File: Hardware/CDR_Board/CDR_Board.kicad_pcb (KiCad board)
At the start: 2 copper layers, 61 x 40.6 mm, 55 parts, among them J1 BLE Friend, J2 nRF24L01, J3 Battery, J5 USB_C_Receptacle_USB2.0, Q1 DMP2045U, SW1 BOOTSEL, SW2 RESET, U1 W25Q32JVSS, U2 SOT23-5 200mA 3.3V, U3 RP2040, U4 BQ25172, U6 ADXL343, Y1 Crystal

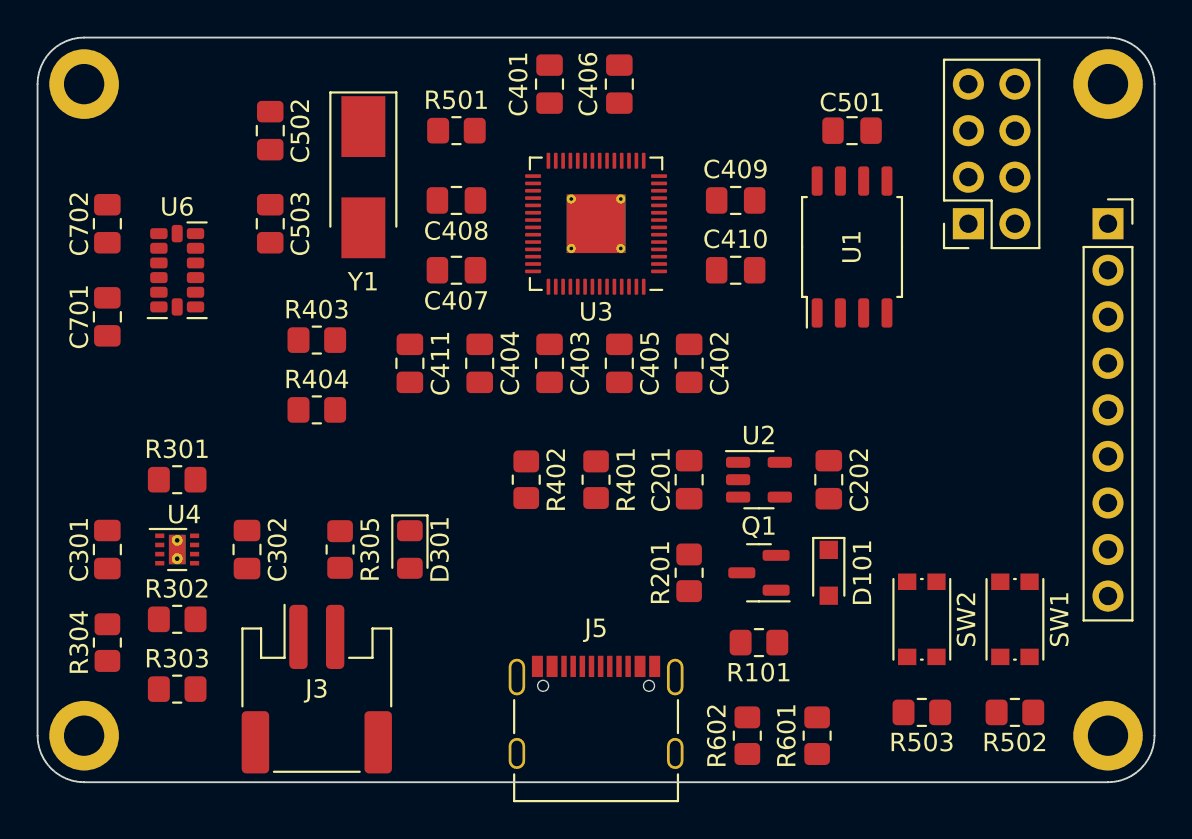
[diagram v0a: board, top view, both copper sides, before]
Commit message: CDR Board Placement Revision
Some things on 25 mil grid, 0603 capacitors for RP2040 decoupling.
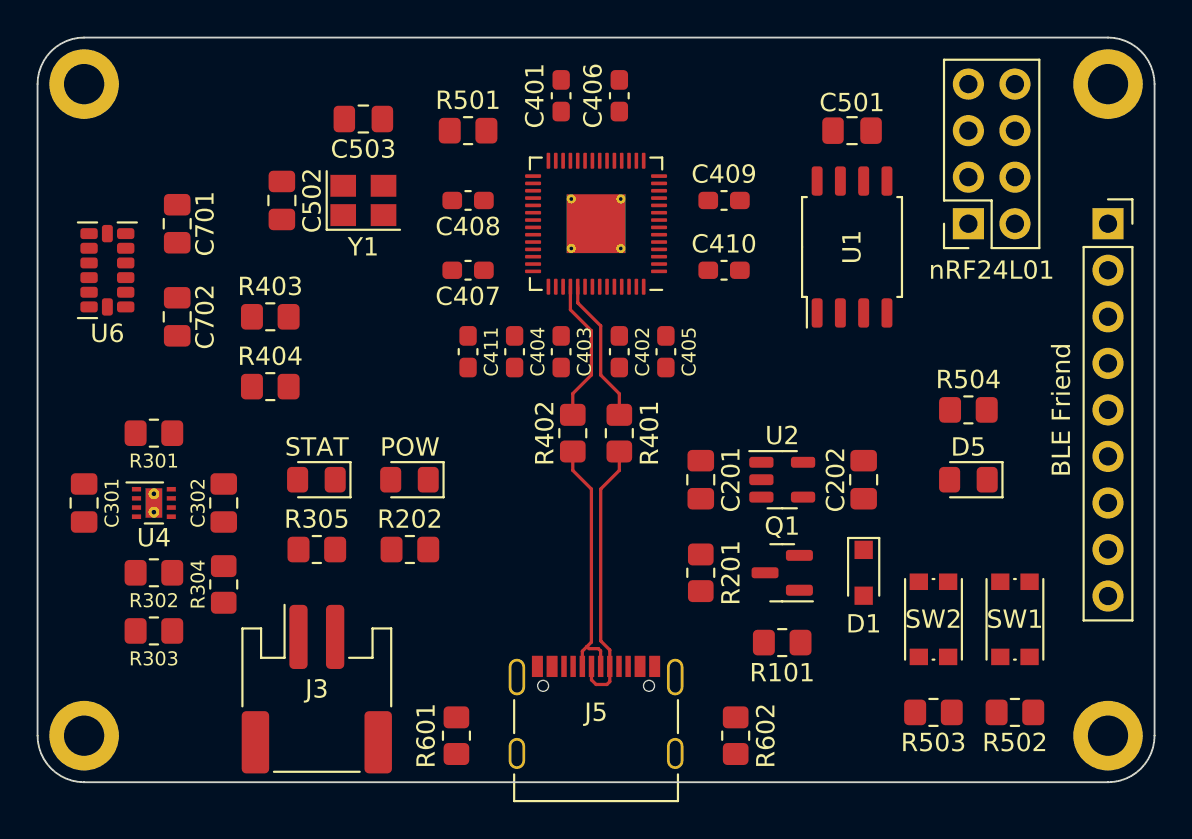
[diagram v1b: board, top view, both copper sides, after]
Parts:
- removed D101: SMB ≥20V ≥1A, Diode_SMD:D_SOD-323_HandSoldering
- removed D301: LED, LED_SMD:LED_0805_2012Metric_Pad1.15x1.40mm_HandSolder
- added D1: SMB ≥20V ≥1A, Diode_SMD:D_SOD-323_HandSoldering, F.Cu at (167.0, 105.4)
- added D2: LED, LED_SMD:LED_0805_2012Metric_Pad1.15x1.40mm_HandSolder, F.Cu at (137.1, 100.3)
- added D3: GPIO, LED_SMD:LED_0805_2012Metric_Pad1.15x1.40mm_HandSolder, F.Cu at (172.7, 100.3)
- added D4: POW, LED_SMD:LED_0805_2012Metric_Pad1.15x1.40mm_HandSolder, F.Cu at (142.2, 100.3)
- added R202: 330, Resistor_SMD:R_0805_2012Metric_Pad1.20x1.40mm_HandSolder, F.Cu at (142.2, 104.1)
- added R504: 330, Resistor_SMD:R_0805_2012Metric_Pad1.20x1.40mm_HandSolder, F.Cu at (172.7, 96.5)
- C401, C402, C403, C404, C405, C406, C407, C408, C409, C410, C411: footprint Capacitor_SMD:C_0805_2012Metric_Pad1.18x1.45mm_HandSolder -> Capacitor_SMD:C_0603_1608Metric_Pad1.08x0.95mm_HandSolder
- Y1: footprint Crystal:Crystal_SMD_Abracon_ABM3-2Pin_5.0x3.2mm_HandSoldering -> Crystal:Crystal_SMD_SeikoEpson_FA238-4Pin_3.2x2.5mm
- moved R601 19.7 mm to (144.8, 114.3)
- moved C503 7.65 mm to (139.7, 80.6), turned to 0 degrees
- moved R304 7.10 mm to (132.1, 106.0), turned to -90 degrees
- moved C701 6.35 mm to (129.5, 86.4), turned to -90 degrees
- moved C702 6.35 mm to (129.5, 91.4), turned to 90 degrees
- moved C402 3.86 mm to (153.7, 93.3)
- moved C502 3.86 mm to (135.3, 85.1)
- moved U6 3.81 mm to (125.7, 88.9), turned to 180 degrees
- moved R402 3.59 mm to (151.1, 97.8)
- moved R303 3.42 mm to (128.3, 108.6)
- moved C411 3.24 mm to (145.4, 93.3)
- moved C301 2.84 mm to (124.5, 101.6)
- moved C302 2.84 mm to (132.1, 101.6)
- moved R302 2.84 mm to (128.3, 105.4)
- moved U4 2.84 mm to (128.3, 101.6)
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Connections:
- Y1 pad 2: Net-(C503-Pad2) -> GND
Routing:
- net /D+: track 0.00 -> 15.1 mm
- net /D-: track 0.00 -> 14.0 mm
- net Net-(R401-Pad1): track 0.00 -> 7.93 mm
- net Net-(R402-Pad1): track 0.00 -> 7.89 mm
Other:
- board text added: "BLE Friend"
- board text added: "D5"
- board text added: "POW"
- board text added: "STAT"
- board text added: "nRF24L01"

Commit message: Added critical traces
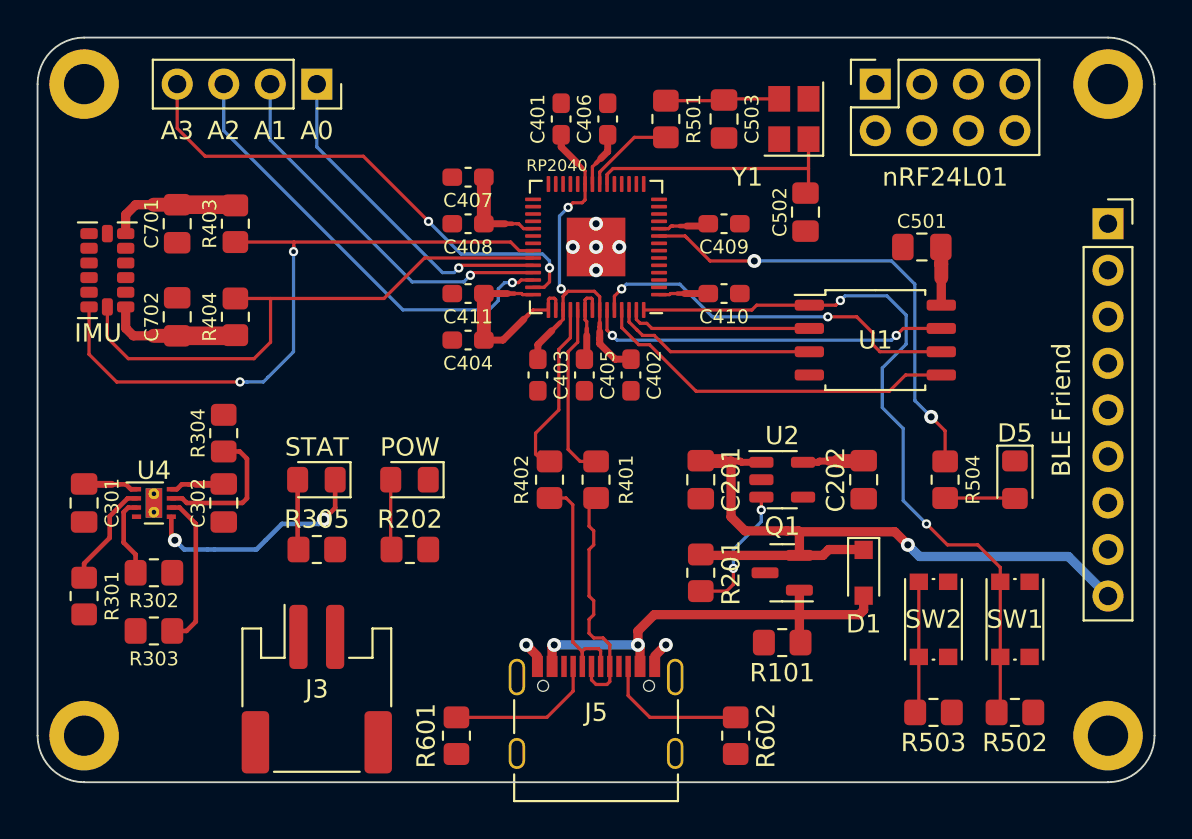
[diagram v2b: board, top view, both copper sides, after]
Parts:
- added J4: ADC, Connector_PinSocket_2.54mm:PinSocket_1x04_P2.54mm_Vertical, F.Cu at (137.2, 78.7)
- U3: footprint Package_DFN_QFN:QFN-56-1EP_7x7mm_P0.4mm_EP3.2x3.2mm_ThermalVias -> Package_DFN_QFN:QFN-56-1EP_7x7mm_P0.4mm_EP3.2x3.2mm
- moved C502 28.6 mm to (163.8, 85.7), turned to 90 degrees
- moved Y1 23.9 mm to (163.2, 80.6), turned to 90 degrees
- moved C503 19.7 mm to (159.4, 80.6), turned to 90 degrees
- moved R501 10.8 mm to (156.2, 80.6), turned to -90 degrees
- moved R301 9.67 mm to (124.5, 106.7), turned to -90 degrees
- moved J2 9.16 mm to (167.6, 78.7), turned to 90 degrees
- moved R304 8.25 mm to (132.1, 97.8)
- moved C501 7.41 mm to (170.2, 87.6), turned to 0 degrees
- moved R403 5.43 mm to (132.7, 86.4), turned to -90 degrees
- moved U1 5.24 mm to (167.6, 92.7), turned to 0 degrees
- moved C407 5.08 mm to (145.4, 83.8)
- moved C405 4.62 mm to (151.8, 94.6)
- moved R404 4.26 mm to (132.7, 91.4), turned to 90 degrees
- moved R504 4.02 mm to (171.4, 100.3), turned to 90 degrees
- moved C411 3.17 mm to (145.4, 90.2), turned to 180 degrees
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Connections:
- J1 pad 1: unconnected-(J1-Pad1) -> /SCK
- J1 pad 2: unconnected-(J1-Pad2) -> /MISO
- J1 pad 3: unconnected-(J1-Pad3) -> /MOSI
- J1 pad 4: unconnected-(J1-Pad4) -> /BLE_CS
- J1 pad 5: unconnected-(J1-Pad5) -> /BLE_IRQ
- J1 pad 8: unconnected-(J1-Pad8) -> GND
- J1 pad 9: unconnected-(J1-Pad9) -> /VSRC
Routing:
- net +3V3: track 0.00 -> 50.6 mm
- net /BOOT/FLASH_CS: track 0.00 -> 41.0 mm, vias 0 -> 2
- net /VSRC: track 0.00 -> 39.1 mm, vias 0 -> 1
- net /SDA: track 0.00 -> 37.5 mm, vias 0 -> 2
- net /SCL: track 0.00 -> 31.0 mm
- net /A3: track 0.00 -> 27.9 mm, vias 0 -> 2
- net VBUS: track 0.00 -> 27.3 mm, vias 0 -> 2
- net /D5: track 0.00 -> 25.4 mm, vias 0 -> 2
- net /A2: track 0.00 -> 24.5 mm, vias 0 -> 1
- net +1V1: track 0.00 -> 21.1 mm, vias 0 -> 2
- net /A1: track 0.00 -> 20.8 mm, vias 0 -> 1
- net /FLASH_CLK: track 0.00 -> 20.8 mm, vias 0 -> 2
- net Net-(U1-Pad5): track 0.00 -> 20.2 mm
- net Net-(U1-Pad7): track 0.00 -> 19.8 mm, vias 0 -> 2
- net /A0: track 0.00 -> 18.2 mm, vias 0 -> 1
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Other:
- board text added: "A0"
- board text added: "A1"
- board text added: "A2"
- board text added: "A3"
- board text added: "IMU"
- board text added: "RP2040"

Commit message: Finished all routing
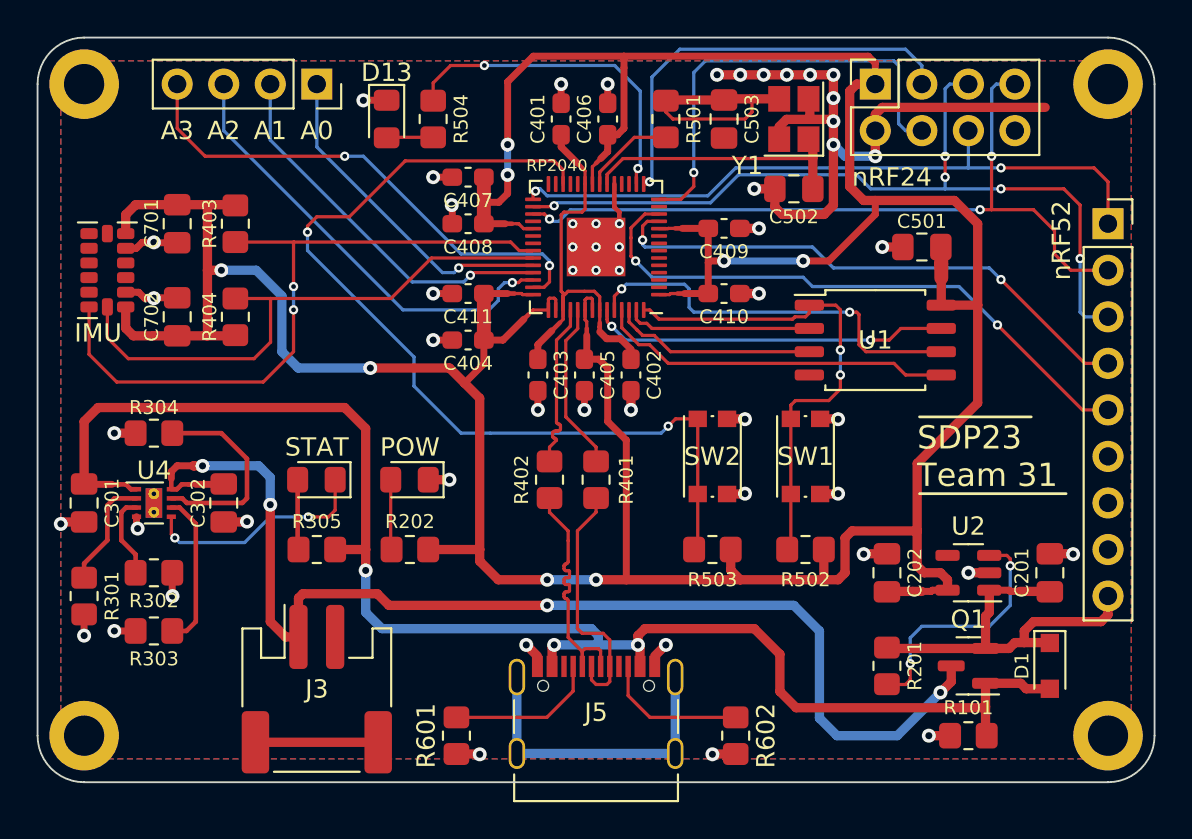
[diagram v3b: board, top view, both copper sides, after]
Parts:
- D2: value LED -> STAT
- moved D3 39.5 mm to (141.0, 80.6)
- moved R504 34.2 mm to (143.5, 80.6)
- moved C201 19.7 mm to (177.2, 105.4), turned to 90 degrees
- moved R503 15.0 mm to (158.8, 104.1)
- moved SW2 15.0 mm to (158.8, 99.1)
- moved R502 14.5 mm to (163.8, 104.1)
- moved SW1 14.5 mm to (163.8, 99.1)
- moved D1 11.4 mm to (177.2, 110.5)
- moved Q1 11.4 mm to (172.7, 110.5)
- moved R101 11.4 mm to (172.7, 114.3)
- moved R201 11.4 mm to (168.3, 110.5)
- moved U2 11.4 mm to (172.7, 105.4), turned to 180 degrees
- moved C202 5.24 mm to (168.3, 105.4), turned to 90 degrees
- moved R304 3.81 mm to (128.3, 97.8), turned to 0 degrees
- moved C502 1.42 mm to (163.2, 84.5), turned to 0 degrees
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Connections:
- J2 pad 1: unconnected-(J2-Pad1) -> +3V3
- J2 pad 2: unconnected-(J2-Pad2) -> GND
- J2 pad 3: unconnected-(J2-Pad3) -> /RF_CNS
- J2 pad 4: unconnected-(J2-Pad4) -> /RF_CE
- J2 pad 5: unconnected-(J2-Pad5) -> /MOSI
- J2 pad 6: unconnected-(J2-Pad6) -> /SCK
- J2 pad 7: unconnected-(J2-Pad7) -> /MISO
- R504 pad 2: /D5 -> /D13
- U3 pad 11: /D6 -> /BLE_CS
- U3 pad 12: /D9 -> /BLE_IRQ
- U3 pad 14: /D11 -> /RF_CE
- U3 pad 15: /D12 -> /RF_CNS
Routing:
- net +3V3: track 50.6 -> 223.3 mm, vias 0 -> 8
- net GND: track 2.85 -> 83.8 mm, vias 7 -> 55
- net +BATT: track 2.98 -> 65.4 mm, vias 0 -> 4
- net VBUS: track 27.3 -> 84.1 mm, vias 2 -> 3
- net /MOSI: track 0.00 -> 45.6 mm, vias 0 -> 5
- net /RUN: track 7.21 -> 51.6 mm, vias 0 -> 2
- net /MISO: track 0.00 -> 41.9 mm, vias 0 -> 3
- net /SCK: track 0.00 -> 37.2 mm, vias 0 -> 2
- net /BLE_IRQ: track 0.00 -> 32.9 mm, vias 0 -> 2
- net /BLE_CS: track 0.00 -> 30.1 mm, vias 0 -> 2
- net /D5: track 25.4 -> 0.00 mm, vias 2 -> 0
- net /RF_CE: track 0.00 -> 24.6 mm, vias 0 -> 1
- net /RF_CNS: track 0.00 -> 22.9 mm, vias 0 -> 1
- net /D13: track 0.00 -> 18.4 mm, vias 0 -> 2
- net unconnected-(J5-PadS1): track 0.00 -> 17.0 mm
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- added copper zone on B.Cu, net GND
- added copper zone on F.Cu, net GND
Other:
- board text added: "D13"
- board text added: "SDP23 Team 31"
- board text added: "nRF24"
- board text added: "nRF52"
- board text removed: "BLE Friend"
- board text removed: "D5"
- board text removed: "nRF24L01"

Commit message: Added stitching vias
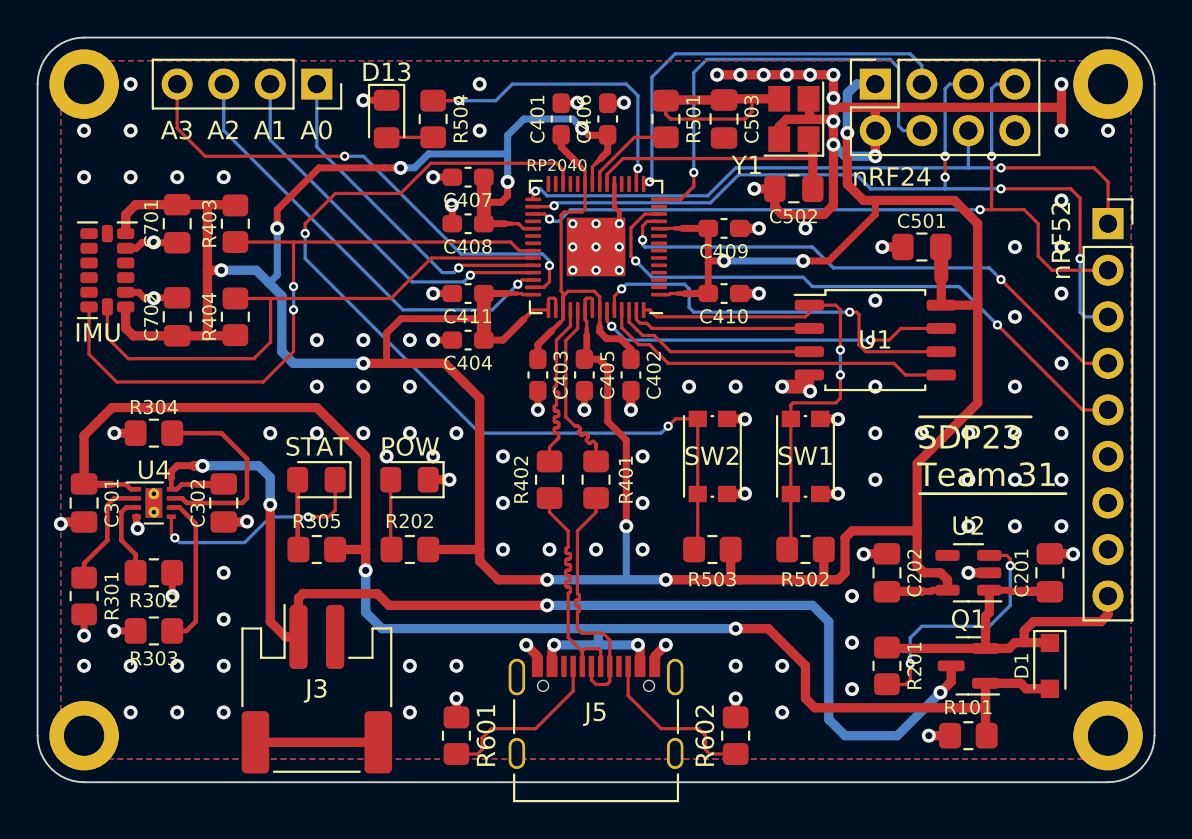
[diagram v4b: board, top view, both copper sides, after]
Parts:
- turned R601 to -90 degrees
- turned R602 to -90 degrees
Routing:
- net unconnected-(J5-PadS1): track 17.0 -> 0.00 mm
- net GND: track 83.8 -> 91.4 mm, vias 55 -> 132
- net /D13: track 18.4 -> 16.7 mm
- net Net-(J5-PadB5): track 7.95 -> 9.23 mm
- net +3V3: track 223.3 -> 222.1 mm, vias 8 -> 12
- net Net-(J5-PadA5): track 8.31 -> 9.51 mm
- net Net-(R401-Pad1): track 9.22 -> 10.1 mm
- net Net-(R402-Pad1): track 9.29 -> 10.1 mm
- net VBUS: track 84.1 -> 84.4 mm, vias 3 -> 4

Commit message: Added more stitching vias
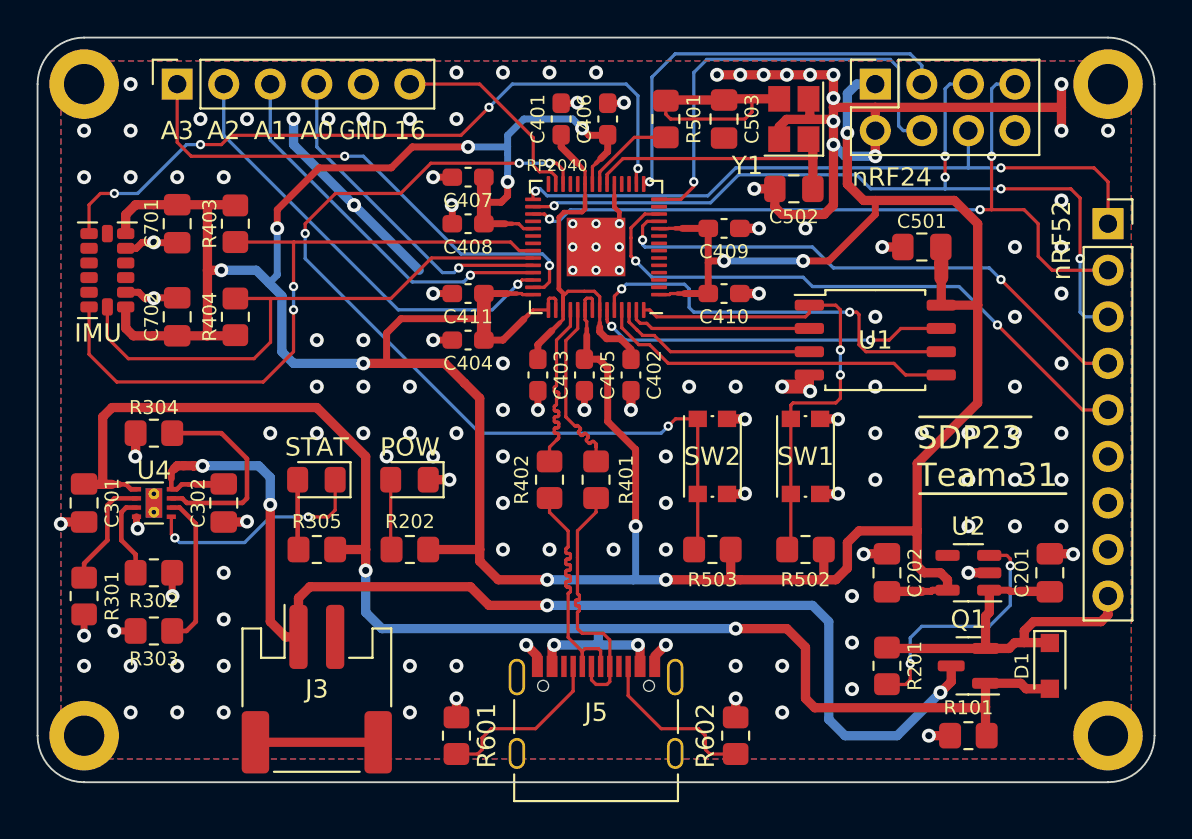
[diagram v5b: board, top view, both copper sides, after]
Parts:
- removed D3: GPIO, LED_SMD:LED_0805_2012Metric_Pad1.15x1.40mm_HandSolder
- removed R504: 330, Resistor_SMD:R_0805_2012Metric_Pad1.20x1.40mm_HandSolder
- J1: value BLE Friend -> nRF52
- J2: value nRF24L01 -> nRF24
- J4: value ADC -> Conn_01x06; footprint Connector_PinSocket_2.54mm:PinSocket_1x04_P2.54mm_Vertical -> Connector_PinSocket_2.54mm:PinSocket_1x06_P2.54mm_Vertical
- moved J4 7.62 mm to (129.5, 78.7), turned to 90 degrees
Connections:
- J4 pad 1: /A0 -> /A3
- J4 pad 2: /A1 -> /A2
- J4 pad 3: /A2 -> /A1
- J4 pad 4: /A3 -> /A0
- U3 pad 27: unconnected-(U3-Pad27) -> /GPIO16
- U6 pad 8: unconnected-(U6-Pad8) -> /D13
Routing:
- net /D13: track 16.7 -> 39.4 mm, vias 2 -> 4
- net /GPIO16: track 0.00 -> 11.4 mm
- net GND: track 91.4 -> 101.4 mm, vias 132 -> 142
- net Net-(D3-Pad2): track 2.55 -> 0.00 mm
- net /RUN: vias 2 -> 4
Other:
- board text added: "16"
- board text added: "GND"
- board text removed: "D13"

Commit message: Finalized PCB v1
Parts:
- added R504: DNF, Resistor_SMD:R_0805_2012Metric_Pad1.20x1.40mm_HandSolder, F.Cu at (167.6, 98.0)
- R502: value 10K -> 1K
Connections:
- R502 pad 1: +3V3 -> /FLASH_CS
- R502 pad 2: /BOOT/FLASH_CS -> /~{BOOT}
- SW1 pad 2: /BOOT/FLASH_CS -> /~{BOOT}
- U1 pad 1: /BOOT/FLASH_CS -> /FLASH_CS
- U3 pad 56: /BOOT/FLASH_CS -> /FLASH_CS
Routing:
- net /BOOT/FLASH_CS: track 26.9 -> 0.00 mm, vias 2 -> 0
- net /FLASH_CS: track 0.00 -> 26.1 mm, vias 0 -> 2
- net /~{BOOT}: track 0.00 -> 6.93 mm
- net VBUS: track 84.7 -> 82.2 mm
- net /D-: track 14.2 -> 12.0 mm
- net +3V3: track 222.3 -> 224.2 mm
- net GND: track 101.4 -> 103.1 mm, vias 142 -> 139
- net Net-(R301-Pad1): track 6.23 -> 6.74 mm
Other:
- board text added: "SDP23 Team 31: Helmet Board v1 JLCJLCJLCJLC A. Sahay, M. Morel, M.P. Gonzalez, R. Patel Prof. Arbabi"
- board text added: "SMH"
